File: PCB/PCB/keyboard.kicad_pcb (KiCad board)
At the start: 2 copper layers, 369.9 x 122.3 mm, 223 parts, among them SW1 SW_PUSH, SW2 SW_PUSH, U1 STM32F072CBUx, U2 MCP1700-3302E_SOT23

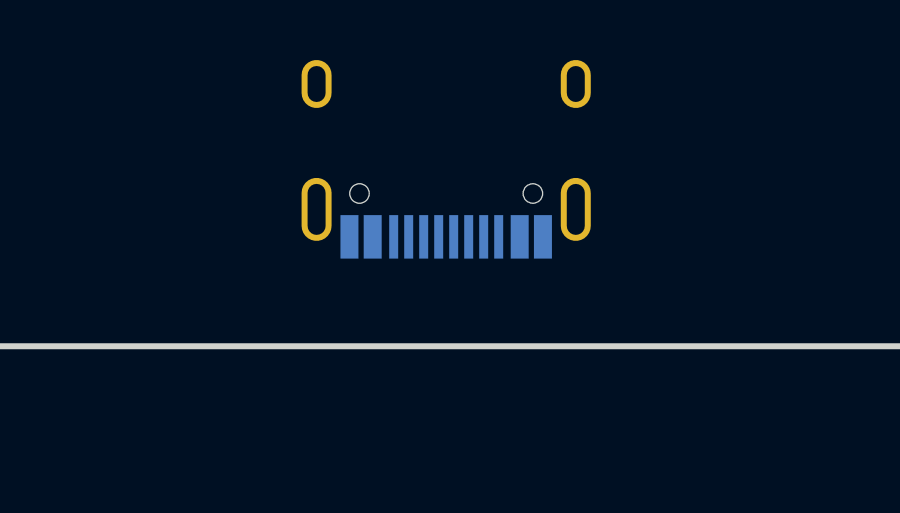
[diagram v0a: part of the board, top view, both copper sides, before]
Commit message: Top Plate Started
Still need to add cutouts for Plate and get dimensions for F-Row blockers
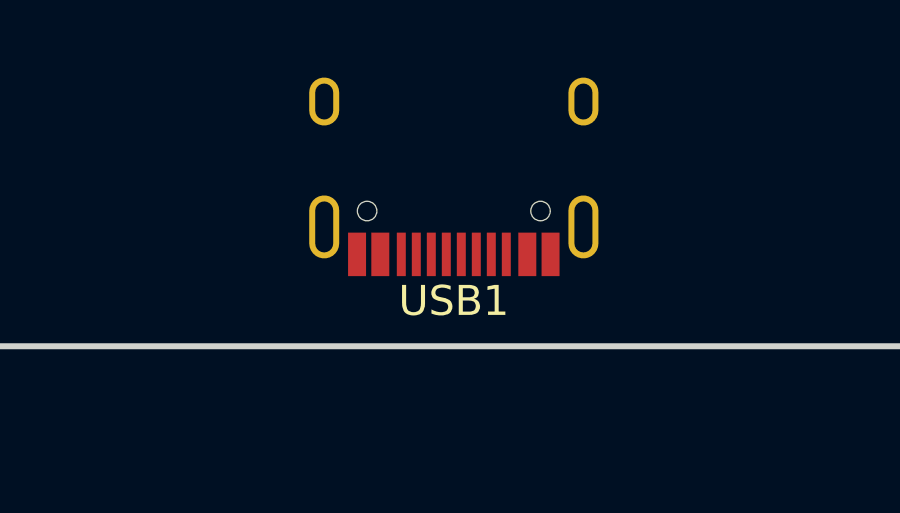
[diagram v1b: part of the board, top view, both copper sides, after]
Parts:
- USB1: moved to F.Cu
- moved USB1 0.64 mm to (20.9, -14.8), turned to 180 degrees
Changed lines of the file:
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@@
     (add_net row5)
   )
-  (module Type-C:HRO-TYPE-C-31-M-12 (layer B.Cu)
-    (at 20.6756 -15.3416)
+  (module Type-C:HRO-TYPE-C-31-M-12 (layer F.Cu)
+    (at 20.9296 -14.7574 180)
     (attr smd)
-    (fp_text reference USB1 (at 0 9.25) (layer B.SilkS)
-      (effects (font (size 1 1) (thickness 0.15)) (justify mirror))
+    (fp_text reference USB1 (at 0 -9.25) (layer F.SilkS)
+      (effects (font (size 1 1) (thickness 0.15)))
     )
-    (fp_text value HRO-TYPE-C-31-M-12 (at 0 -1.15) (layer Dwgs.User)
+    (fp_text value HRO-TYPE-C-31-M-12 (at 0 1.15) (layer Dwgs.User)
       (effects (font (size 1 1) (thickness 0.15)))
     )
     (fp_line (start -4.47 0) (end 4.47 0) (layer Dwgs.User) (width 0.15))
-    (fp_line (start -4.47 0) (end -4.47 7.3) (layer Dwgs.User) (width 0.15))
-    (fp_line (start 4.47 0) (end 4.47 7.3) (layer Dwgs.User) (width 0.15))
-    (fp_line (start -4.47 7.3) (end 4.47 7.3) (layer Dwgs.User) (width 0.15))
-    (pad 12 smd rect (at 3.225 7.695) (size 0.6 1.45) (layers B.Cu B.Paste B.Mask)
+    (fp_line (start -4.47 0) (end -4.47 -7.3) (layer Dwgs.User) (width 0.15))
+    (fp_line (start 4.47 0) (end 4.47 -7.3) (layer Dwgs.User) (width 0.15))
+    (fp_line (start -4.47 -7.3) (end 4.47 -7.3) (layer Dwgs.User) (width 0.15))
+    (pad 12 smd rect (at 3.225 -7.695 180) (size 0.6 1.45) (layers F.Cu F.Paste F.Mask)
       (net 1 GND))
-    (pad 1 smd rect (at -3.225 7.695) (size 0.6 1.45) (layers B.Cu B.Paste B.Mask)
+    (pad 1 smd rect (at -3.225 -7.695 180) (size 0.6 1.45) (layers F.Cu F.Paste F.Mask)
       (net 1 GND))
-    (pad 11 smd rect (at 2.45 7.695) (size 0.6 1.45) (layers B.Cu B.Paste B.Mask)
+    (pad 11 smd rect (at 2.45 -7.695 180) (size 0.6 1.45) (layers F.Cu F.Paste F.Mask)
       (net 130 "Net-(F1-Pad2)"))
-    (pad 2 smd rect (at -2.45 7.695) (size 0.6 1.45) (layers B.Cu B.Paste B.Mask)
+    (pad 2 smd rect (at -2.45 -7.695 180) (size 0.6 1.45) (layers F.Cu F.Paste F.Mask)
       (net 130 "Net-(F1-Pad2)"))
-    (pad 3 smd rect (at -1.75 7.695) (size 0.3 1.45) (layers B.Cu B.Paste B.Mask)
+    (pad 3 smd rect (at -1.75 -7.695 180) (size 0.3 1.45) (layers F.Cu F.Paste F.Mask)
       (net 172 "Net-(USB1-Pad3)"))
-    (pad 10 smd rect (at 1.75 7.695) (size 0.3 1.45) (layers B.Cu B.Paste B.Mask)
+    (pad 10 smd rect (at 1.75 -7.695 180) (size 0.3 1.45) (layers F.Cu F.Paste F.Mask)
       (net 134 "Net-(R5-Pad1)"))
-    (pad 4 smd rect (at -1.25 7.695) (size 0.3 1.45) (layers B.Cu B.Paste B.Mask)
+    (pad 4 smd rect (at -1.25 -7.695 180) (size 0.3 1.45) (layers F.Cu F.Paste F.Mask)
       (net 133 "Net-(R4-Pad1)"))
-    (pad 9 smd rect (at 1.25 7.695) (size 0.3 1.45) (layers B.Cu B.Paste B.Mask)
+    (pad 9 smd rect (at 1.25 -7.695 180) (size 0.3 1.45) (layers F.Cu F.Paste F.Mask)
       (net 173 "Net-(USB1-Pad9)"))
-    (pad 5 smd rect (at -0.75 7.695) (size 0.3 1.45) (layers B.Cu B.Paste B.Mask)
+    (pad 5 smd rect (at -0.75 -7.695 180) (size 0.3 1.45) (layers F.Cu F.Paste F.Mask)
       (net 146 D-))
-    (pad 8 smd rect (at 0.75 7.695) (size 0.3 1.45) (layers B.Cu B.Paste B.Mask)
+    (pad 8 smd rect (at 0.75 -7.695 180) (size 0.3 1.45) (layers F.Cu F.Paste F.Mask)
       (net 145 D+))
-    (pad 7 smd rect (at 0.25 7.695) (size 0.3 1.45) (layers B.Cu B.Paste B.Mask)
+    (pad 7 smd rect (at 0.25 -7.695 180) (size 0.3 1.45) (layers F.Cu F.Paste F.Mask)
       (net 146 D-))
-    (pad 6 smd rect (at -0.25 7.695) (size 0.3 1.45) (layers B.Cu B.Paste B.Mask)
+    (pad 6 smd rect (at -0.25 -7.695 180) (size 0.3 1.45) (layers F.Cu F.Paste F.Mask)
       (net 145 D+))
-    (pad "" np_thru_hole circle (at 2.89 6.25) (size 0.65 0.65) (drill 0.65) (layers *.Cu *.Mask))
-    (pad "" np_thru_hole circle (at -2.89 6.25) (size 0.65 0.65) (drill 0.65) (layers *.Cu *.Mask))
-    (pad 13 thru_hole oval (at -4.32 6.78) (size 1 2.1) (drill oval 0.6 1.7) (layers *.Cu F.Mask)
+    (pad "" np_thru_hole circle (at 2.89 -6.25 180) (size 0.65 0.65) (drill 0.65) (layers *.Cu *.Mask))
+    (pad "" np_thru_hole circle (at -2.89 -6.25 180) (size 0.65 0.65) (drill 0.65) (layers *.Cu *.Mask))
+    (pad 13 thru_hole oval (at -4.32 -6.78 180) (size 1 2.1) (drill oval 0.6 1.7) (layers *.Cu B.Mask)
       (net 129 "Net-(C10-Pad2)"))
-    (pad 13 thru_hole oval (at 4.32 6.78) (size 1 2.1) (drill oval 0.6 1.7) (layers *.Cu F.Mask)
+    (pad 13 thru_hole oval (at 4.32 -6.78 180) (size 1 2.1) (drill oval 0.6 1.7) (layers *.Cu B.Mask)
       (net 129 "Net-(C10-Pad2)"))
-    (pad 13 thru_hole oval (at -4.32 2.6) (size 1 1.6) (drill oval 0.6 1.2) (layers *.Cu F.Mask)
+    (pad 13 thru_hole oval (at -4.32 -2.6 180) (size 1 1.6) (drill oval 0.6 1.2) (layers *.Cu B.Mask)
       (net 129 "Net-(C10-Pad2)"))
-    (pad 13 thru_hole oval (at 4.32 2.6) (size 1 1.6) (drill oval 0.6 1.2) (layers *.Cu F.Mask)
+    (pad 13 thru_hole oval (at 4.32 -2.6 180) (size 1 1.6) (drill oval 0.6 1.2) (layers *.Cu B.Mask)
       (net 129 "Net-(C10-Pad2)"))
   )

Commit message: V2 CAD finished.
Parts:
- removed D_90: D, Diode_SMD:D_SOD-123
- C1: value 100nF -> 10nF
- C2: value 4.7uF -> 100nF; footprint Capacitor_SMD:C_0603_1608Metric -> Capacitor_SMD:C_0402_1005Metric
- C7: value 10nF -> 4.7uF; footprint Capacitor_SMD:C_0402_1005Metric -> Capacitor_SMD:C_0603_1608Metric
- K_0, K_1, K_10, K_100, K_11, K_12, K_13, K_14, K_15, K_16, K_17, K_18, K_19, K_2, K_20, K_21, K_22, K_23, K_24, K_25, K_26, K_27, K_28, K_29, K_3, K_30, K_32, K_33, K_34, K_35, K_37, K_38, K_39, K_4, K_40, K_41, K_42, K_43, K_44, K_45, K_46, K_47, K_48, K_5, K_50, K_51, K_52, K_55, K_56, K_57, K_58, K_59, K_6, K_60, K_61, K_62, K_63, K_64, K_65, K_67, K_68, K_69, K_7, K_71, K_72, K_73, K_74, K_75, K_76, K_77, K_78, K_79, K_8, K_80, K_82, K_83, K_84, K_85, K_9, K_96, K_97, K_98, K_99: footprint MX_Alps_Hybrid:MX-1U-NoLED -> MX_Only:MXOnly-1U-NoLED
- K_31: footprint MX_Alps_Hybrid:MX-2U-NoLED -> MX_Only:MXOnly-2U-NoLED
- K_36, K_49: footprint MX_Alps_Hybrid:MX-1.5U-NoLED -> MX_Only:MXOnly-1.5U-NoLED
- K_53, K_86: footprint MX_Alps_Hybrid:MX-1U-NoLED -> MX_Only:MXOnly-2U-NoLED
- K_54, K_81: footprint MX_Alps_Hybrid:MX-1.75U-NoLED -> MX_Only:MXOnly-1.75U-NoLED
- K_66, K_70, K_91: footprint MX_Alps_Hybrid:MX-2.25U-NoLED -> MX_Only:MXOnly-2.25U-NoLED
- K_87, K_88, K_89, K_92, K_94, K_95: footprint MX_Alps_Hybrid:MX-1.25U-NoLED -> MX_Only:MXOnly-1.25U-NoLED
- K_90: footprint MX_Alps_Hybrid:MX-6.25U-NoLED -> MX_Only:MXOnly-6.25U-NoLED
- K_93: footprint MX_Alps_Hybrid:MX-2.753U-NoLED -> MX_Only:MXOnly-2.75U-NoLED
- moved U1 155.4 mm to (277.9, 188.7)
- moved C7 144.9 mm to (284.9, 186.4), turned to 90 degrees
- moved C3 144.6 mm to (283.5, 187.0), turned to 90 degrees
- moved C4 140.8 mm to (279.7, 194.4)
- moved C2 136.8 mm to (276.2, 183.1), turned to 180 degrees
- moved C6 136.3 mm to (275.6, 181.0), turned to 180 degrees
- moved D_53 130.8 mm to (447.2, 146.4)
- moved C5 130.7 mm to (272.2, 191.6), turned to 270 degrees
- moved D_86 130.7 mm to (447.2, 184.4)
- moved K_86 128.5 mm to (442.1, 177.8), turned to 270 degrees
- moved K_53 128.5 mm to (442.1, 139.7), turned to 270 degrees
- moved C1 127.7 mm to (273.4, 191.6), turned to 270 degrees
- moved USB1 127.3 mm to (111.1, 75.1)
- moved D_52 126.1 mm to (431.8, 136.5)
- moved D_85 126.1 mm to (431.8, 174.6)
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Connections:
- U1 pad 1: +3V3 -> Net-(U1-Pad1)
- U1 pad 10: Net-(U1-Pad10) -> row0
- U1 pad 13: Net-(U1-Pad13) -> col0
- U1 pad 14: Net-(U1-Pad14) -> col1
- U1 pad 15: Net-(U1-Pad15) -> col2
- U1 pad 16: Net-(U1-Pad16) -> col3
- U1 pad 17: Net-(U1-Pad17) -> col4
- U1 pad 18: Net-(U1-Pad18) -> col5
- U1 pad 19: Net-(U1-Pad19) -> col6
- U1 pad 2: Net-(U1-Pad2) -> row5
- U1 pad 20: Net-(U1-Pad20) -> col7
- U1 pad 21: Net-(U1-Pad21) -> col8
- U1 pad 22: Net-(U1-Pad22) -> col9
- U1 pad 3: Net-(U1-Pad3) -> row4
- U1 pad 37: Net-(U1-Pad37) -> col10
- U1 pad 38: Net-(U1-Pad38) -> col11
- U1 pad 39: Net-(U1-Pad39) -> col12
- U1 pad 4: Net-(U1-Pad4) -> row3
- U1 pad 40: Net-(U1-Pad40) -> col13
- U1 pad 41: Net-(U1-Pad41) -> col14
- U1 pad 42: Net-(U1-Pad42) -> col15
- U1 pad 43: Net-(U1-Pad43) -> col16
- U1 pad 45: Net-(U1-Pad45) -> col17
- U1 pad 46: Net-(U1-Pad46) -> col18
- U1 pad 5: Net-(U1-Pad5) -> row2
- U1 pad 6: Net-(U1-Pad6) -> row1
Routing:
- net row0: track 0.00 -> 646.9 mm
- net row1: track 0.00 -> 618.7 mm
- net row2: track 0.00 -> 587.7 mm
- net row3: track 0.00 -> 569.5 mm
- net row5: track 0.00 -> 542.3 mm
- net row4: track 0.00 -> 529.3 mm
- net GND: track 0.00 -> 395.5 mm, vias 0 -> 5
- net +3V3: track 0.00 -> 344.6 mm, vias 0 -> 9
- net col0: track 0.00 -> 286.9 mm
- net D+: track 0.00 -> 278.8 mm, vias 0 -> 3
- net D-: track 0.00 -> 278.1 mm, vias 0 -> 3
- net col18: track 0.00 -> 269.1 mm, vias 0 -> 1
- net col1: track 0.00 -> 268.7 mm, vias 0 -> 1
- net col2: track 0.00 -> 249.1 mm, vias 0 -> 1
- net col17: track 0.00 -> 242.6 mm, vias 0 -> 1
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- added copper zone on B.Cu, net GND
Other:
- board size 369.9 x 122.3 mm -> 368.2 x 122.7 mm
- net class Default: trace_width 0.25 -> 0.254
- net class Power added: clearance 0.2, trace_width 0.3048, via_dia 0.8, via_drill 0.4

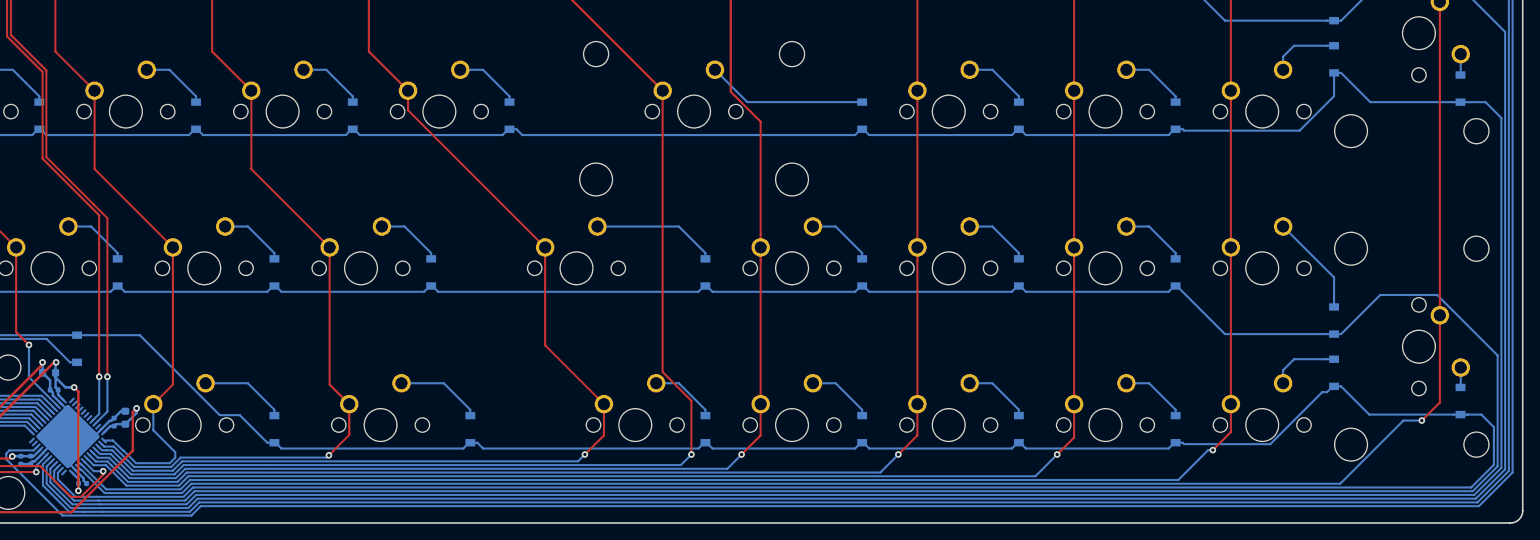
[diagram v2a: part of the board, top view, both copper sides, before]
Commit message: Updates to PCB
Moved Numpad + and Enter diodes.
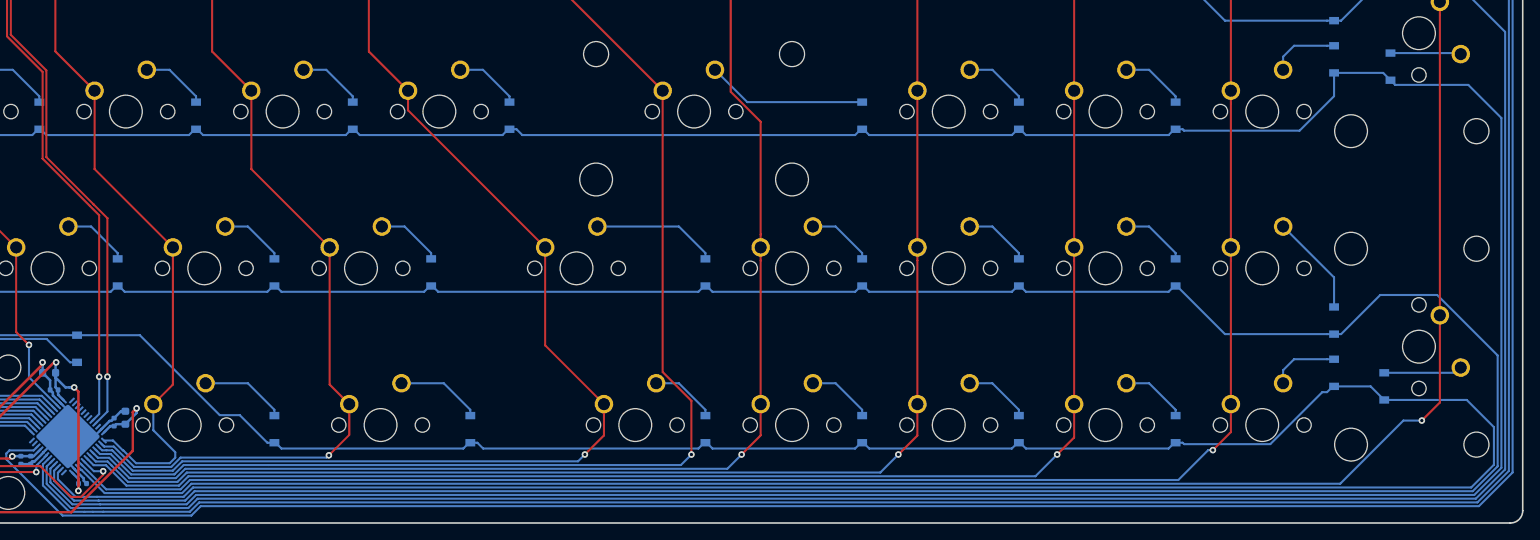
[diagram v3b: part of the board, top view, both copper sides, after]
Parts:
- moved D_86 9.44 mm to (437.9, 182.6)
- moved D_53 8.92 mm to (438.7, 143.8)
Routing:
- net Net-(D_86-Pad2): track 2.43 -> 9.57 mm
- net Net-(D_53-Pad2): track 2.55 -> 8.59 mm

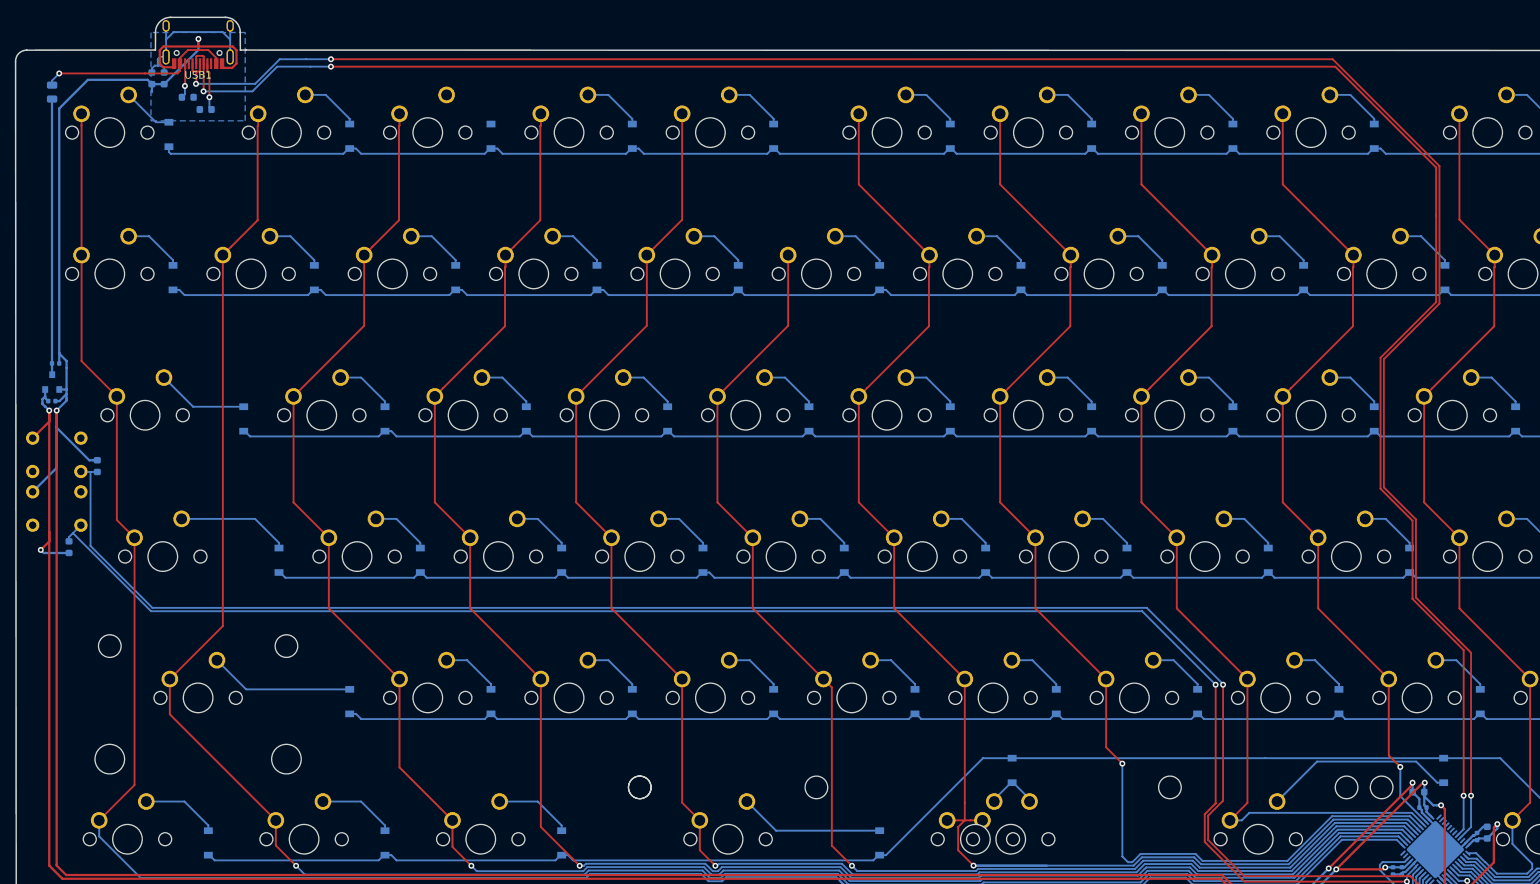
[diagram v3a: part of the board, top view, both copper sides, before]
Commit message: Added ESD Protection to PCB
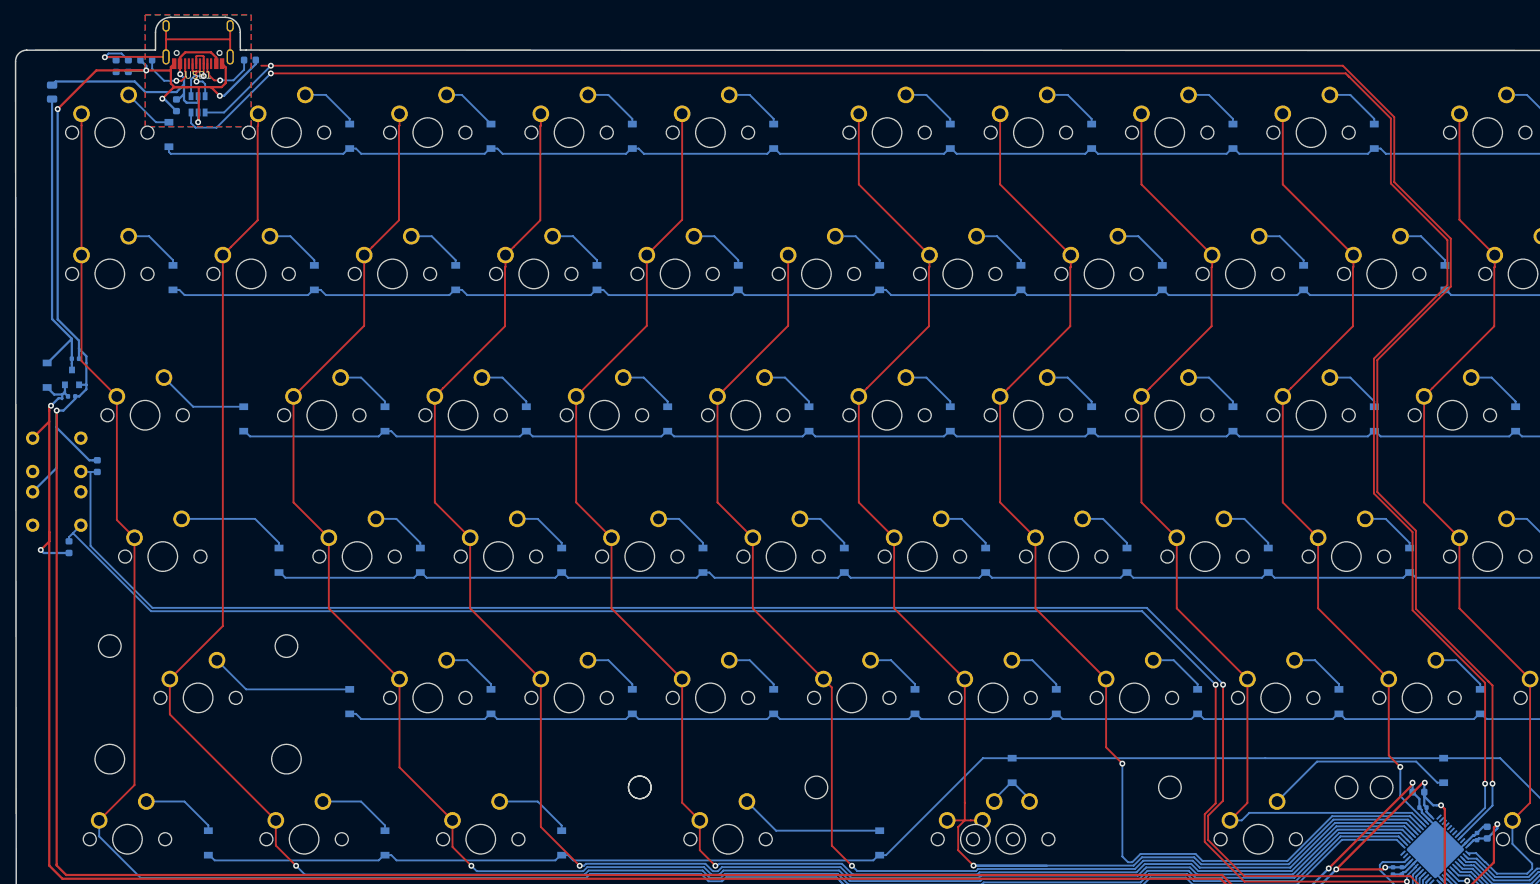
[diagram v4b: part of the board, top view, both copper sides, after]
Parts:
- added C11: 100nF, Capacitor_SMD:C_0603_1608Metric, B.Cu at (108.2, 88.4)
- added D1: D_Schottky, Diode_SMD:D_SOD-123, B.Cu at (90.8, 124.8)
- added U3: USBLC6-2SC6, Package_TO_SOT_SMD:SOT-23-6, B.Cu at (111.1, 88.3)
- C8, C9: value 1uF -> 0.1uF
- moved R4 8.95 mm to (118.1, 82.3), turned to 0 degrees
- moved R5 7.51 mm to (104.1, 82.3), turned to 180 degrees
- moved C10 5.10 mm to (100.1, 83.1)
- moved R3 5.10 mm to (101.7, 83.1)
- moved C9 2.74 mm to (94.1, 127.6)
- moved U2 2.74 mm to (94.1, 125.1)
- moved C8 2.74 mm to (94.6, 122.6)
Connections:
- net Net-(F1-Pad2) renamed VBUS
- USB1 pad 5: D- -> DBus-
- USB1 pad 6: D+ -> DBus+
- USB1 pad 7: D- -> DBus-
- USB1 pad 8: D+ -> DBus+
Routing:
- net GND: track 395.5 -> 412.1 mm, vias 5 -> 9
- net DBus-: track 0.00 -> 8.85 mm, vias 0 -> 1
- net VBUS: track 26.7 -> 35.5 mm
- net Net-(C10-Pad2): track 23.0 -> 30.7 mm, vias 0 -> 1
- net Net-(D_2-Pad2): track 0.00 -> 7.61 mm
- net DBus+: track 0.00 -> 7.31 mm, vias 0 -> 1
- net +5V: track 37.2 -> 42.3 mm
- net Net-(R5-Pad1): track 4.71 -> 8.37 mm
- net D-: track 278.1 -> 281.0 mm, vias 3 -> 2
- net +3V3: track 344.6 -> 346.9 mm
- net Net-(R4-Pad1): track 6.41 -> 8.55 mm
- net D+: track 278.8 -> 279.8 mm, vias 3 -> 2
- added copper zone on F.Cu, net GND
